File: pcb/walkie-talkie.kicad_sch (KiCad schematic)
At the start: 2 parts

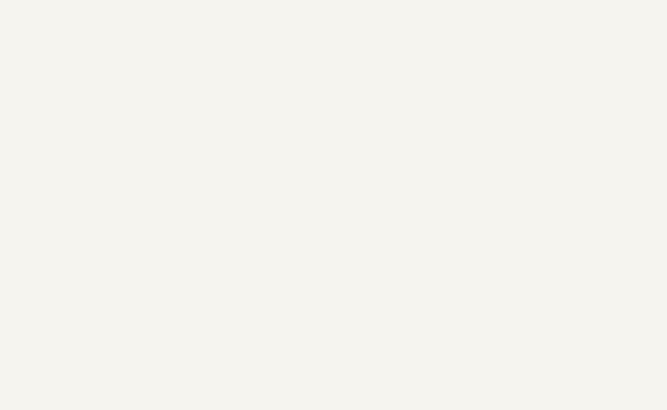
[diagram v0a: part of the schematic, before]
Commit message: Add start of USB power circuit
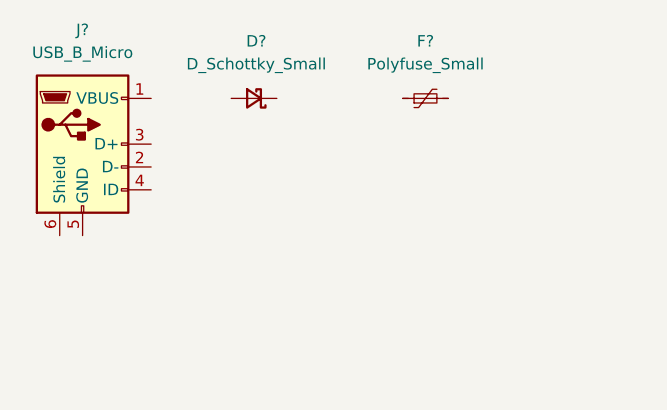
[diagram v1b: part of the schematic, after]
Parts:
- added D?: D_Schottky_Small, symbol Device:D_Schottky_Small
- added F?: Polyfuse_Small, symbol Device:Polyfuse_Small
- added J?: USB_B_Micro, symbol Connector:USB_B_Micro
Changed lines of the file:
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@@
 (kicad_sch (version 20211123) (generator eeschema)
   (paper "A4")
+  (symbol (lib_id "Device:Polyfuse_Small") (at 67.31 26.67 90) (unit 1)
+    (in_bom yes) (on_board yes) (fields_autoplaced)
+    (property "Reference" "F?" (id 0) (at 67.31 20.32 90))
+    (property "Value" "Polyfuse_Small" (id 1) (at 67.31 22.86 90))
+    (property "Footprint" "" (id 2) (at 72.39 25.4 0)
+      (effects (font (size 1.27 1.27)) (justify left) hide)
+    )
+    (property "Datasheet" "~" (id 3) (at 67.31 26.67 0)
+      (effects (font (size 1.27 1.27)) hide)
+    )
+    (pin "1")
+    (pin "2")
+  )
+  (symbol (lib_id "Device:D_Schottky_Small") (at 48.26 26.67 180) (unit 1)
+    (in_bom yes) (on_board yes) (fields_autoplaced)
+    (property "Reference" "D?" (id 0) (at 48.514 20.32 0))
+    (property "Value" "D_Schottky_Small" (id 1) (at 48.514 22.86 0))
+    (property "Footprint" "" (id 2) (at 48.26 26.67 90)
+      (effects (font (size 1.27 1.27)) hide)
+    )
+    (property "Datasheet" "~" (id 3) (at 48.26 26.67 90)
+      (effects (font (size 1.27 1.27)) hide)
+    )
+    (pin "1")
+    (pin "2")
+  )
+  (symbol (lib_id "Connector:USB_B_Micro") (at 29.21 31.75 0) (unit 1)
+    (in_bom yes) (on_board yes) (fields_autoplaced)
+    (property "Reference" "J?" (id 0) (at 29.21 19.05 0))
+    (property "Value" "USB_B_Micro" (id 1) (at 29.21 21.59 0))
+    (property "Footprint" "" (id 2) (at 33.02 33.02 0)
+      (effects (font (size 1.27 1.27)) hide)
+    )
+    (property "Datasheet" "~" (id 3) (at 33.02 33.02 0)
+      (effects (font (size 1.27 1.27)) hide)
+    )
+    (pin "1")
+    (pin "2")
+    (pin "3")
+    (pin "4")
+    (pin "5")
+    (pin "6")
+  )
   (symbol (lib_id "Audio:PCM5102") (at 233.68 50.8 0) (unit 1)
     (in_bom yes) (on_board yes) (fields_autoplaced)
@@
   )
   (symbol_instances
+    (path "/7b6b9719-0278-4b64-9346-be03bcec0686"
+      (reference "D?") (unit 1) (value "D_Schottky_Small") (footprint "")
+    )
+    (path "/258807b1-d2d0-4e3c-9143-902d2155e67d"
+      (reference "F?") (unit 1) (value "Polyfuse_Small") (footprint "")
+    )
+    (path "/9a84d94f-20bd-48b2-9507-16c84791a59e"
+      (reference "J?") (unit 1) (value "USB_B_Micro") (footprint "")
+    )
     (path "/cf89533d-ed9d-47a8-9bf7-db1237da3977"
       (reference "U?") (unit 1) (value "PCM5102") (footprint "Package_SO:TSSOP-20_4.4x6.5mm_P0.65mm")

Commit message: Connect voltage regulator
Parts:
- added C? (x2): 1uF, symbol Device:C_Small
- added U?: RT9080-33GJ5, footprint:TSOT-23-5_L2.9-W1.6-P0.95-LS2.8-BL, symbol rt9080-33gj5:RT9080-33GJ5
- D?: value D_Schottky_Small -> C8598
- F?: value Polyfuse_Small -> BSMD0805-100-6V
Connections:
- net at F?.1: now also D?.1 (K)
- net +5V: now reaches F?.2
- net +5V: now also C?.1, U?.1 (VIN), U?.3 (EN)
- net at D?.2 (A): now also J?.1 (VBUS)
- net GND: now reaches J?.5 (GND)
- net GND: now also C?.2, C?.2, U?.2 (GND)
- new net +3V3: C?.1, U?.5 (VOUT)
- no-connect marks 0 -> 5
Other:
- note added: "USB + Voltage Regulator"
- moved on the sheet: D?, F?, J?

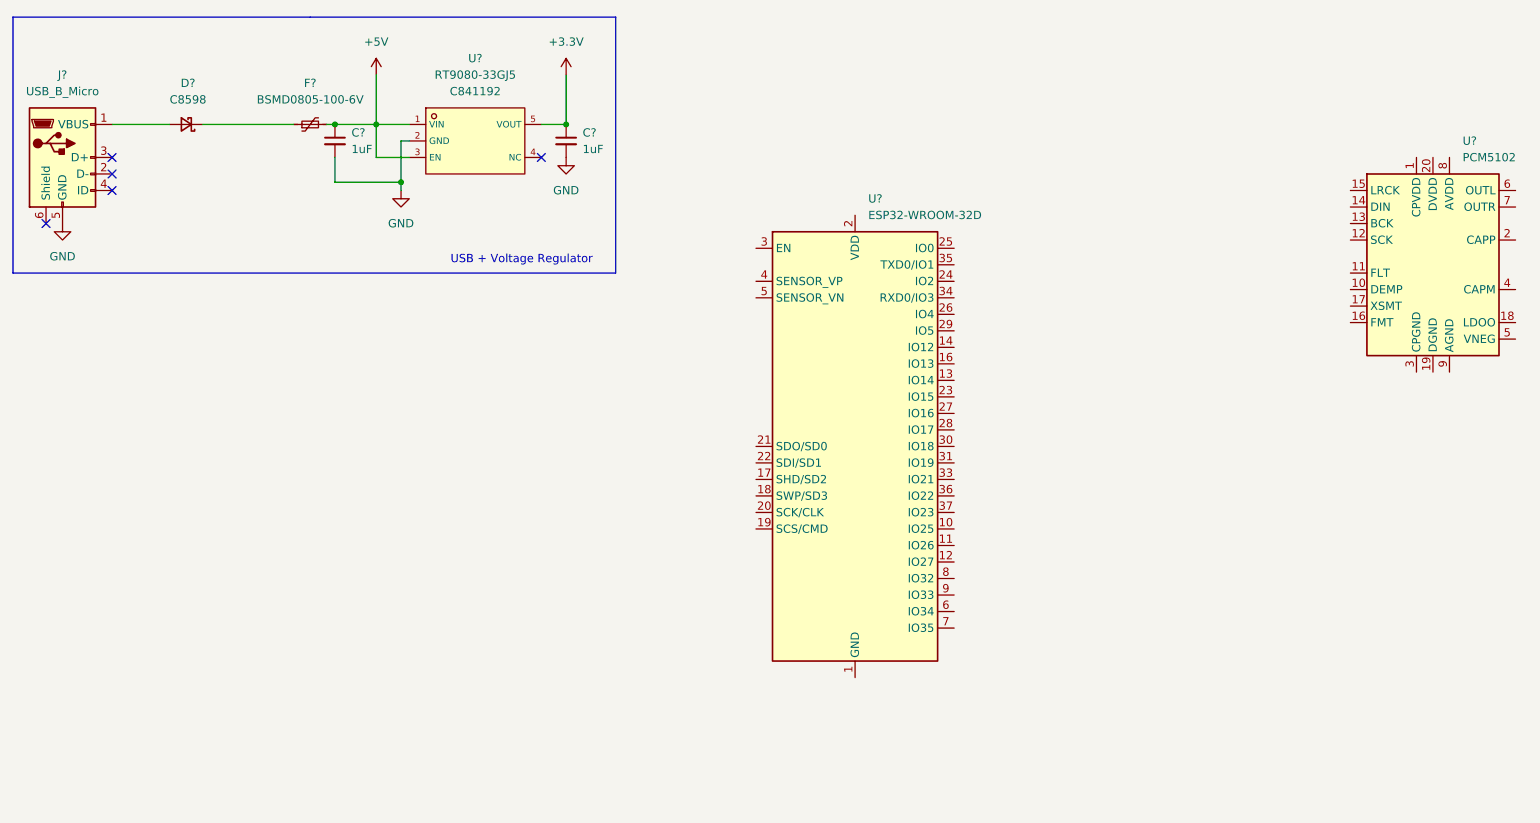
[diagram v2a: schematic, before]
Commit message: Add on/off switch
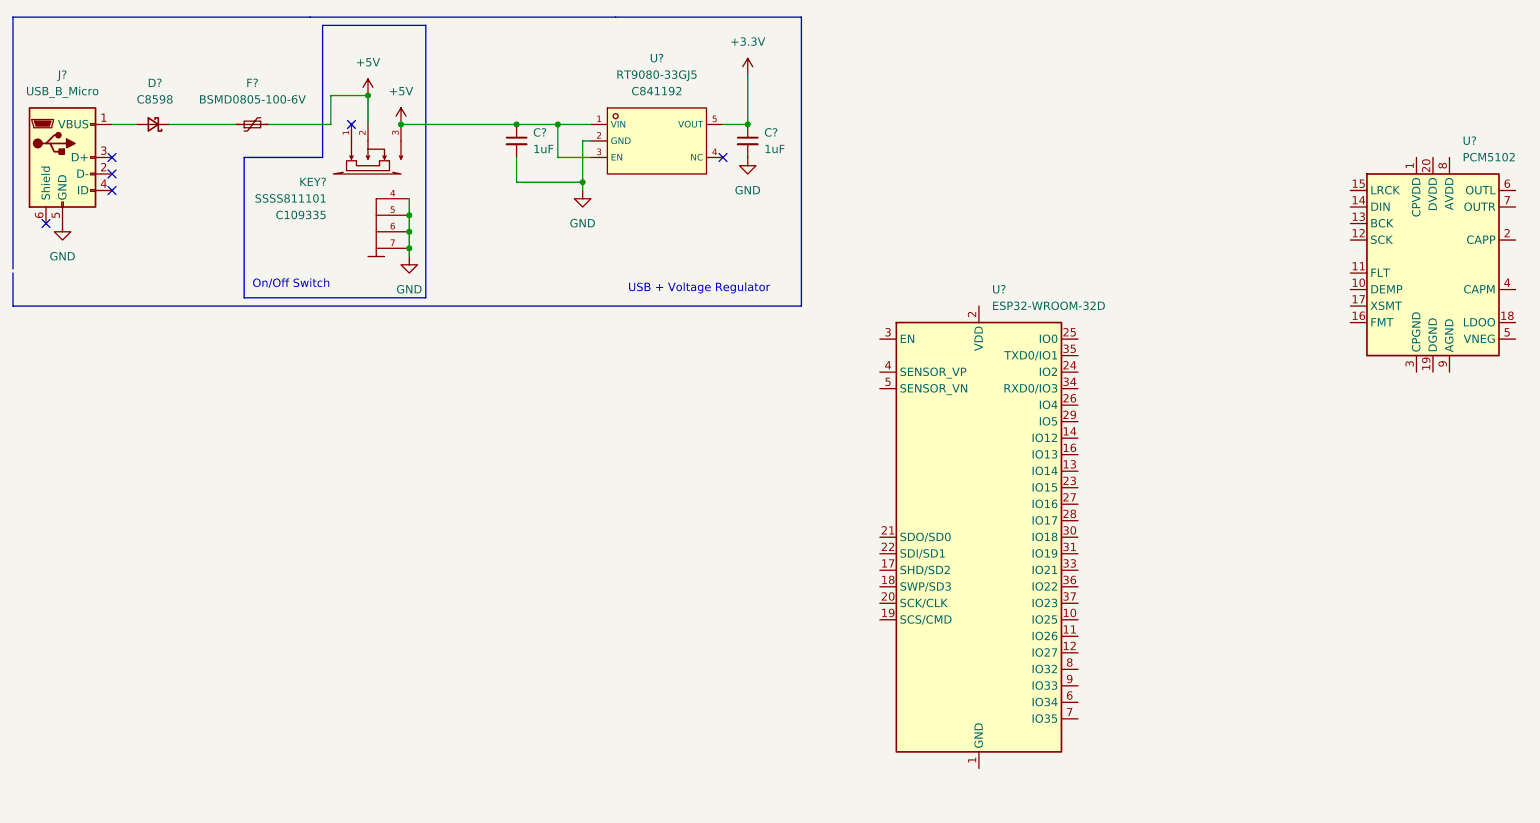
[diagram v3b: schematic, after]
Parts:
- added KEY?: SSSS811101, footprint:SW-SMD_SSSS811101, symbol ssss811101:SSSS811101
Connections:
- net +5V: now also KEY?.2, KEY?.3
- net GND: now also KEY?.4, KEY?.5, KEY?.6, KEY?.7
- no-connect marks 5 -> 6
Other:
- note added: "On/Off Switch"
- moved on the sheet: C?, D?, F?, U?

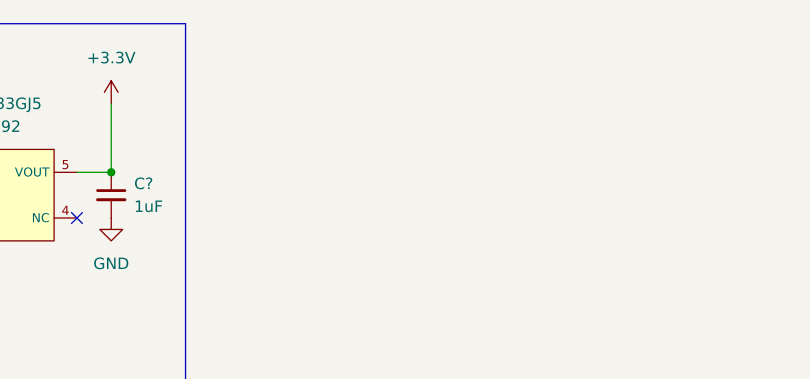
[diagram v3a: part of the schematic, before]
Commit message: Add power LED
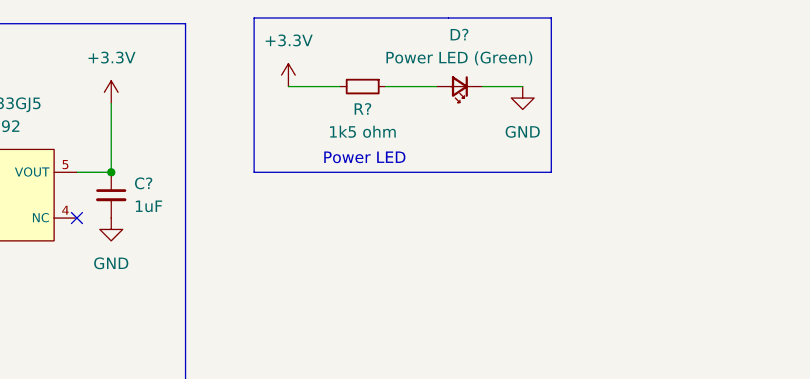
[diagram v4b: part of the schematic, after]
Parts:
- added D?: Power LED (Green), symbol Device:LED_Small
- added R?: 1k5 ohm, symbol Device:R_Small
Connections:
- net +3V3: now also R?.2
- net GND: now also D?.1 (K)
- new net: D?.2 (A), R?.1
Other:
- note added: "Power LED"
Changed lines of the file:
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@@
+    (stroke (width 0) (type default) (color 0 0 0 0))
+  )
+  (polyline (pts (xy 144.145 30.48) (xy 144.145 13.335))
     (stroke (width 0) (type default) (color 0 0 0 0))
   )
@@
     (stroke (width 0) (type default) (color 0 0 0 0))
   )
+  (wire (pts (xy 147.955 20.955) (xy 153.67 20.955))
+    (stroke (width 0) (type default) (color 0 0 0 0))
+  )
+  (wire (pts (xy 169.545 20.955) (xy 173.99 20.955))
+    (stroke (width 0) (type default) (color 0 0 0 0))
+  )
   (wire (pts (xy 102.87 39.37) (xy 102.87 40.64))
     (stroke (width 0) (type default) (color 0 0 0 0))
@@
     (stroke (width 0) (type default) (color 0 0 0 0))
   )
+  (polyline (pts (xy 177.165 13.335) (xy 177.165 30.48))
+    (stroke (width 0) (type default) (color 0 0 0 0))
+  )
   (polyline (pts (xy 50.8 35.56) (xy 62.865 35.56))
     (stroke (width 0) (type default) (color 0 0 0 0))
@@
     (stroke (width 0) (type default) (color 0 0 0 0))
   )
+  (wire (pts (xy 158.75 20.955) (xy 164.465 20.955))
+    (stroke (width 0) (type default) (color 0 0 0 0))
+  )
   (wire (pts (xy 99.06 30.48) (xy 104.14 30.48))
     (stroke (width 0) (type default) (color 0 0 0 0))
   )
+  (polyline (pts (xy 165.735 13.335) (xy 177.165 13.335))
+    (stroke (width 0) (type default) (color 0 0 0 0))
+  )
   (polyline (pts (xy 70.485 15.24) (xy 78.74 15.24))
     (stroke (width 0) (type default) (color 0 0 0 0))
@@
     (stroke (width 0) (type default) (color 0 0 0 0))
   )
+  (polyline (pts (xy 177.165 30.48) (xy 144.145 30.48))
+    (stroke (width 0) (type default) (color 0 0 0 0))
+  )
   (wire (pts (xy 69.85 26.035) (xy 69.85 30.48))
     (stroke (width 0) (type default) (color 0 0 0 0))
   )
+  (polyline (pts (xy 144.145 13.335) (xy 165.735 13.335))
+    (stroke (width 0) (type default) (color 0 0 0 0))
+  )
   (polyline (pts (xy 78.74 15.24) (xy 78.74 57.15))
     (stroke (width 0) (type default) (color 0 0 0 0))
@@
   (wire (pts (xy 128.27 22.86) (xy 128.27 30.48))
     (stroke (width 0) (type default) (color 0 0 0 0))
+  )
+  (text "Power LED" (at 151.765 29.845 0)
+    (effects (font (size 1.27 1.27)) (justify left bottom))
   )
   (text "On/Off Switch" (at 52.07 55.88 0)
@@
     (pin "1")
     (pin "2")
+  )
+  (symbol (lib_id "power:+3.3V") (at 147.955 20.955 0) (unit 1)
+    (in_bom yes) (on_board yes) (fields_autoplaced)
+    (property "Reference" "#PWR?" (id 0) (at 147.955 24.765 0)
+      (effects (font (size 1.27 1.27)) hide)
+    )
+    (property "Value" "+3.3V" (id 1) (at 147.955 15.875 0))
+    (property "Footprint" "" (id 2) (at 147.955 20.955 0)
+      (effects (font (size 1.27 1.27)) hide)
+    )
+    (property "Datasheet" "" (id 3) (at 147.955 20.955 0)
+      (effects (font (size 1.27 1.27)) hide)
+    )
+    (pin "1")
   )
   (symbol (lib_id "ssss811101:SSSS811101") (at 71.12 24.13 0) (unit 1)
@@
     )
     (property "Datasheet" "" (id 3) (at 128.27 22.86 0)
+      (effects (font (size 1.27 1.27)) hide)
+    )
+    (pin "1")
+  )
+  (symbol (lib_id "Device:R_Small") (at 156.21 20.955 270) (unit 1)
+    (in_bom yes) (on_board yes)
+    (property "Reference" "R?" (id 0) (at 156.21 23.495 90))
+    (property "Value" "1k5 ohm" (id 1) (at 156.21 26.035 90))
+    (property "Footprint" "" (id 2) (at 156.21 20.955 0)
+      (effects (font (size 1.27 1.27)) hide)
+    )
+    (property "Datasheet" "~" (id 3) (at 156.21 20.955 0)
+      (effects (font (size 1.27 1.27)) hide)
+    )
+    (pin "1")
+    (pin "2")
+  )
+  (symbol (lib_id "Device:LED_Small") (at 167.005 20.955 180) (unit 1)
+    (in_bom yes) (on_board yes) (fields_autoplaced)
+    (property "Reference" "D?" (id 0) (at 166.9415 15.24 0))
+    (property "Value" "Power LED (Green)" (id 1) (at 166.9415 17.78 0))
+    (property "Footprint" "" (id 2) (at 167.005 20.955 90)
+      (effects (font (size 1.27 1.27)) hide)
+    )
+    (property "Datasheet" "~" (id 3) (at 167.005 20.955 90)
+      (effects (font (size 1.27 1.27)) hide)
+    )
+    (pin "1")
+    (pin "2")
+  )
+  (symbol (lib_id "power:GND") (at 173.99 20.955 0) (unit 1)
+    (in_bom yes) (on_board yes) (fields_autoplaced)
+    (property "Reference" "#PWR?" (id 0) (at 173.99 27.305 0)
+      (effects (font (size 1.27 1.27)) hide)
+    )
+    (property "Value" "GND" (id 1) (at 173.99 26.035 0))
+    (property "Footprint" "" (id 2) (at 173.99 20.955 0)
+      (effects (font (size 1.27 1.27)) hide)
+    )
+    (property "Datasheet" "" (id 3) (at 173.99 20.955 0)
       (effects (font (size 1.27 1.27)) hide)
     )
@@
       (reference "#PWR?") (unit 1) (value "GND") (footprint "")
     )
+    (path "/56c0c712-12e0-4fc4-985b-ba0d439a1b6a"
+      (reference "#PWR?") (unit 1) (value "+3.3V") (footprint "")
+    )
     (path "/825d76ff-a288-419a-a501-231396157ba2"
       (reference "#PWR?") (unit 1) (value "+5V") (footprint "")
@@
       (reference "#PWR?") (unit 1) (value "+3.3V") (footprint "")
     )
+    (path "/f7287042-d4db-4ac7-8863-9cda09046a33"
+      (reference "#PWR?") (unit 1) (value "GND") (footprint "")
+    )
     (path "/4380cac9-0896-438e-8078-13eca543c1a5"
       (reference "C?") (unit 1) (value "1uF") (footprint "")
@@
       (reference "D?") (unit 1) (value "C8598") (footprint "")
     )
+    (path "/f1fa098d-5e48-463e-9873-c04593c740db"
+      (reference "D?") (unit 1) (value "Power LED (Green)") (footprint "")
+    )
     (path "/258807b1-d2d0-4e3c-9143-902d2155e67d"
       (reference "F?") (unit 1) (value "BSMD0805-100-6V") (footprint "")
@@
       (reference "KEY?") (unit 1) (value "SSSS811101") (footprint "footprint:SW-SMD_SSSS811101")
     )
+    (path "/e739e722-5747-422d-a7c7-18e0261ece37"
+      (reference "R?") (unit 1) (value "1k5 ohm") (footprint "")
+    )
     (path "/b1151e5e-5e00-42b1-accd-dc7e4aef562b"
